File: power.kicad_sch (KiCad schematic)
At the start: 30 parts, among them U201 XC6206PxxxMR, U202 XR76208

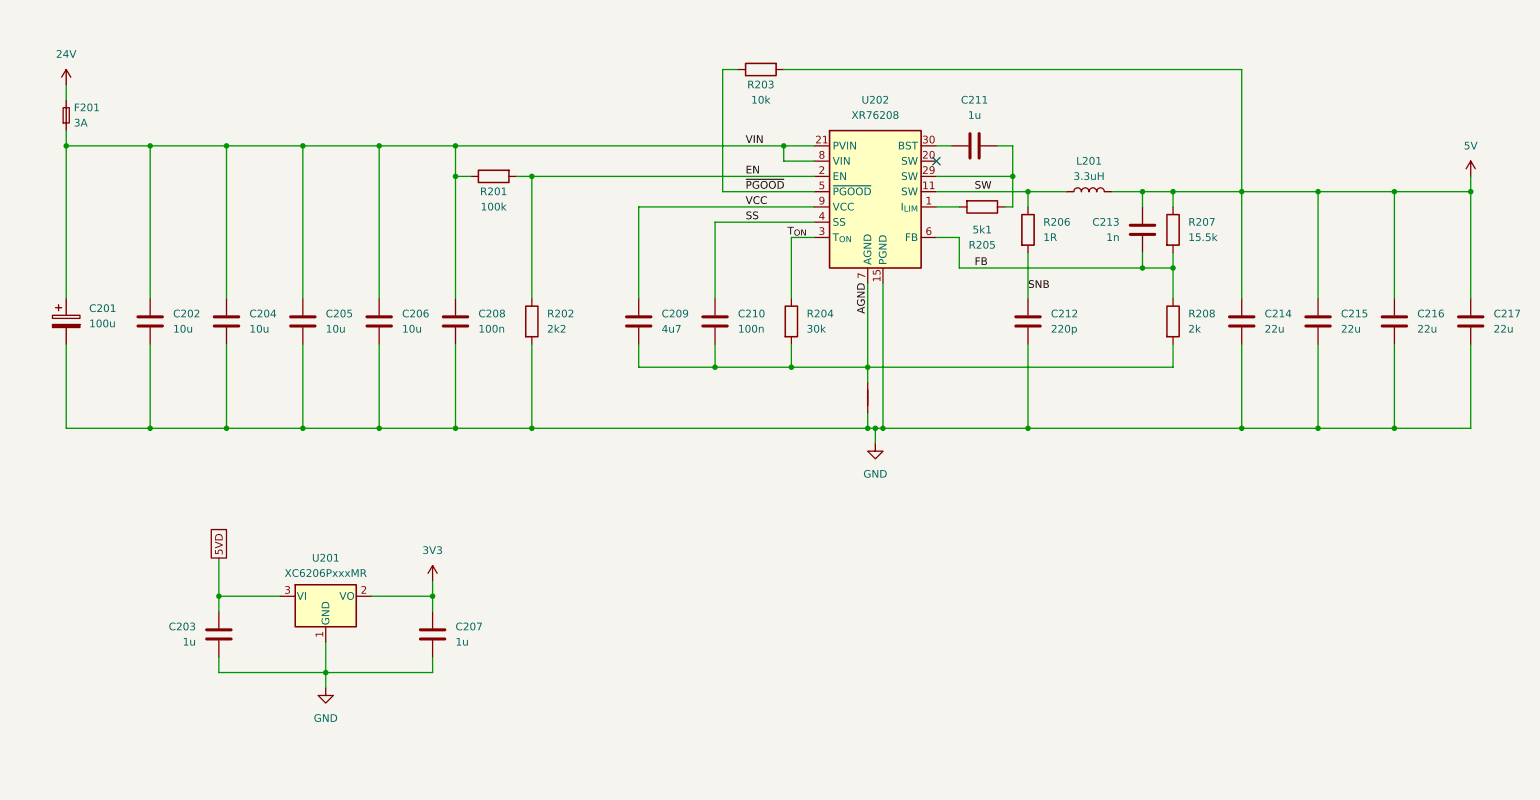
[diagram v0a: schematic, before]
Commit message: Schema improvements and CAN transceiver modification
- Improved schema layout for better readability and organization
- Connected CAN transceiver S-pin to GND for proper operation
- Updated PCB layout to reflect schema changes
- Enhanced component placement and routing clarity
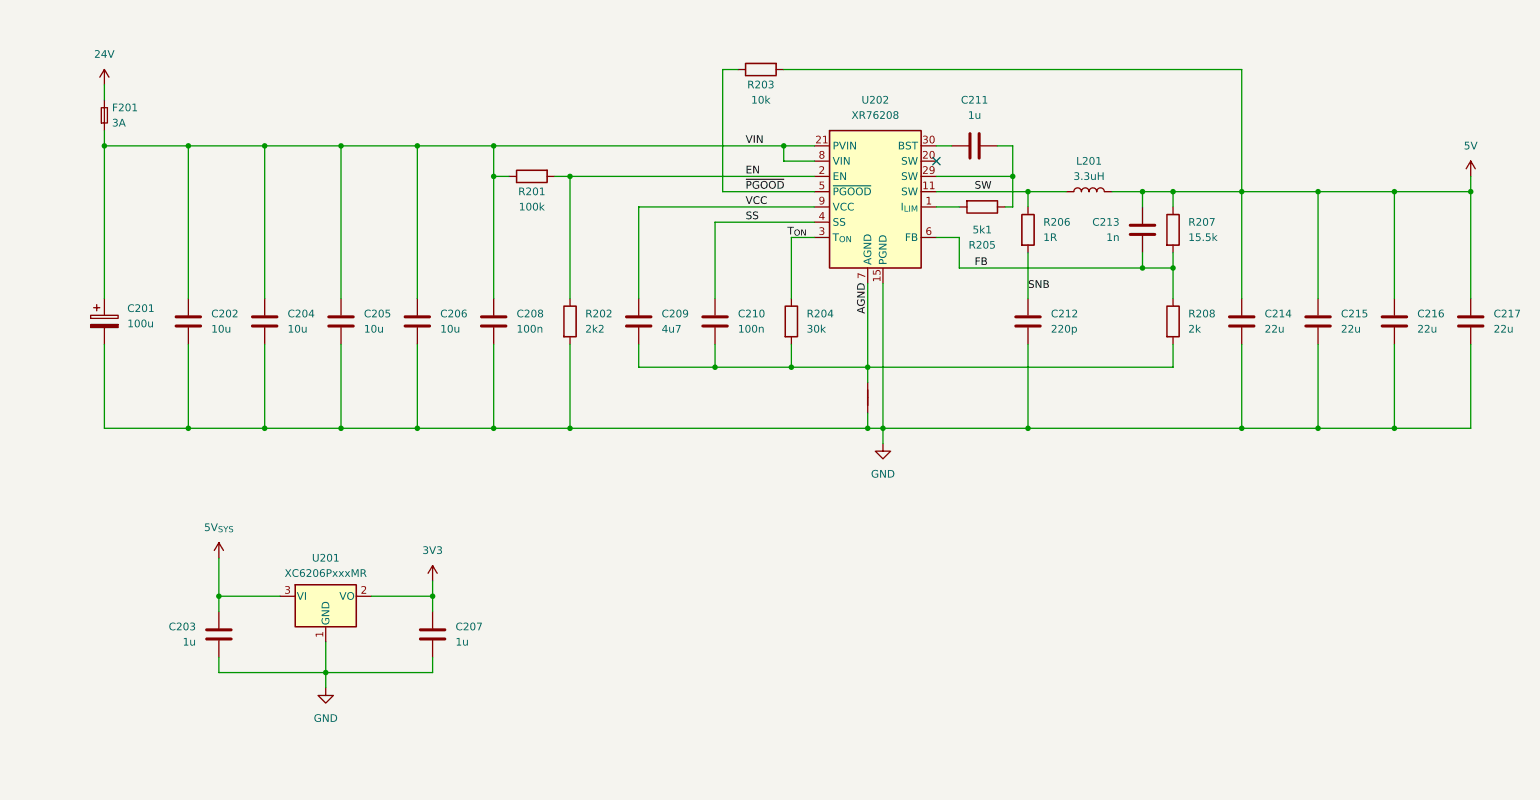
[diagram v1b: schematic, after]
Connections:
- net 5VD renamed 5V_{SYS}
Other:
- moved on the sheet: C201, C202, C204, C205, C206, C208, F201, R201, R202

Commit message: Rev 0.2: Major hardware improvements and production readiness
Hardware Improvements (Thanks to shx for schematic cleanup):
- Clean up schematic organization and structure
- Set CAN transceiver Silent pin to GND for stability
- Add status LEDs (yellow: 24V/5V/3.3V, green: MCU PB4)
- Replace jumpers with solder jumpers on bottom side
- Add jumpers to output PFETs for permanent-on without firmware
- Add robust test points for 5V/GND load testing
- Add optional heatsink for DC/DC converter on bottom
- Add 10µF capacitor for MCU on 3.3V rail

Component Optimizations:
- Replace 30kΩ with 33kΩ basic part for simplified BOM
- Change DC/DC feedback: 15.5kΩ15kΩ (new output: 5.1V)
- Upgrade CAN ESD protection: NUP2105LPESD1CAN
- Increase CAN termination resistor footprint: 04020603
- Switch USB hub supply from 5V to 3.3V per datasheet

Production Ready:
- Add all LCSC part numbers and rotations
- Generate complete production data package
- Improve PCB layout and button placement
- Create comprehensive changelog documentation
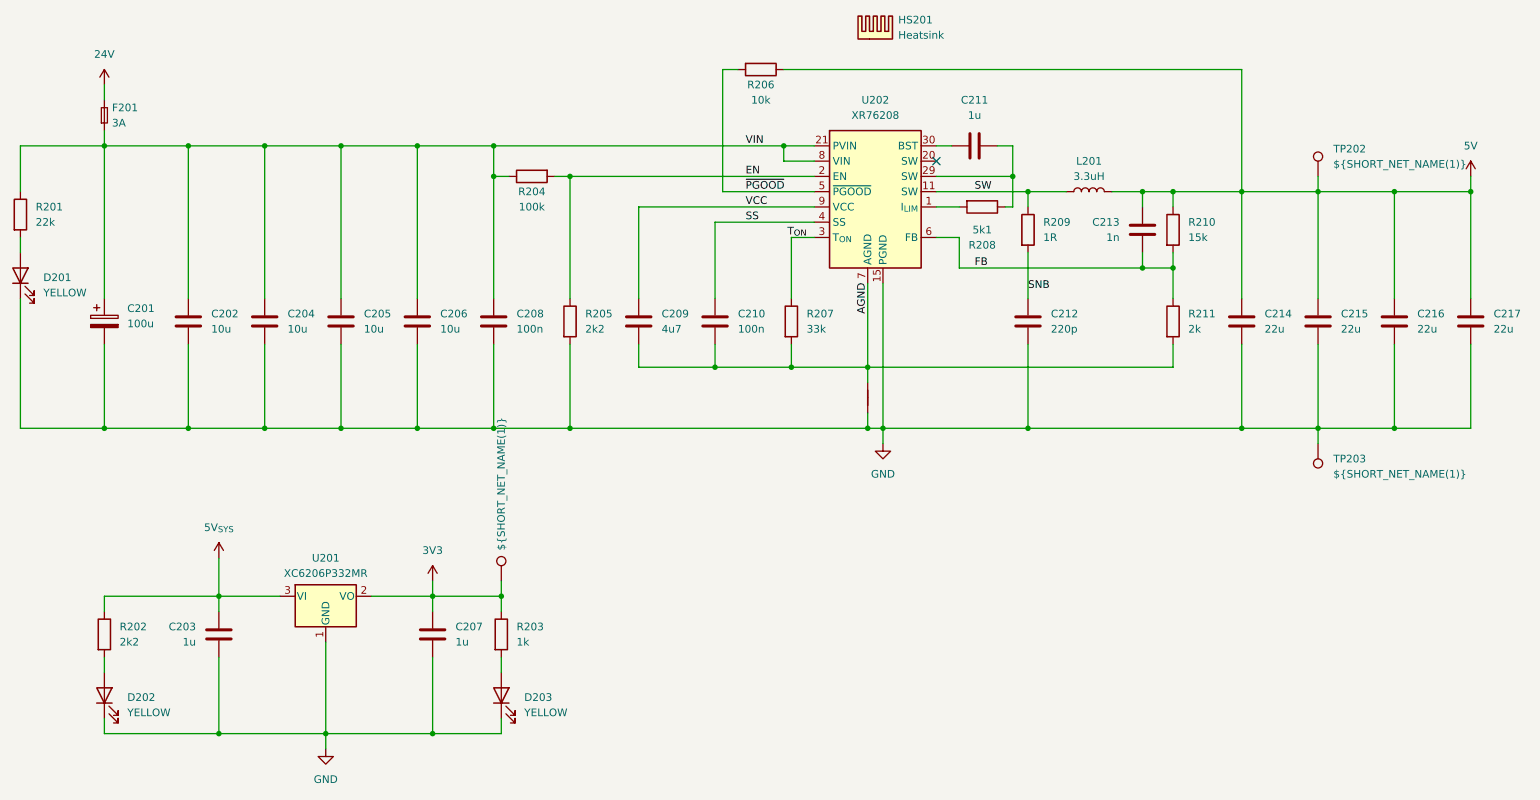
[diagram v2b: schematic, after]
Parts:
- added D201, D202, D203: YELLOW, LED_SMD:LED_0805_2012Metric, symbol Device:LED
- added HS201: Heatsink, project:HeatSink_9x9x5, symbol Mechanical:Heatsink
- added R201: 22k, Resistor_SMD:R_0402_1005Metric, symbol Device:R
- added R202: 2k2, Resistor_SMD:R_0402_1005Metric, symbol Device:R
- added R203: 1k, Resistor_SMD:R_0402_1005Metric, symbol Device:R
- added TP201: ${SHORT_NET_NAME(1)}, project:NAMED_TEST_POINT, symbol project:NamedTestPoint
- added TP202, TP203: ${SHORT_NET_NAME(1)}, TestPoint:TestPoint_Pad_D3.0mm, symbol Connector:TestPoint
- C203, C207, C211: LCSC Part # (none) -> C52923; Manufacturer Part # (none) -> CL05A105KA5NQNC
- C208, C210: LCSC Part # (none) -> C307331; Manufacturer Part # (none) -> CL05B104KB54PNC
- C212: LCSC Part # (none) -> C1603; Manufacturer Part # (none) -> CL10B221KB8NNNC
- C213: LCSC Part # (none) -> C1523; Manufacturer Part # (none) -> 0402B102K500NT
- C214, C215, C216, C217: LCSC Part # (none) -> C12891; Manufacturer Part # (none) -> CL31A226KAHNNNE
- F201: LCSC Part # (none) -> C163126; Manufacturer Part # (none) -> CFS12V3T3R00
- R204: renamed from R201; LCSC Part # (none) -> C25741; Manufacturer Part # (none) -> 0402WGF1003TCE
- R205: renamed from R202; LCSC Part # (none) -> C25879; Manufacturer Part # (none) -> 0402WGF2201TCE
- R206: renamed from R203; LCSC Part # (none) -> C25744; Manufacturer Part # (none) -> 0402WGF1002TCE
- R207: renamed from R204; value 30k -> 33k; LCSC Part # (none) -> C25779; Manufacturer Part # (none) -> 0402WGF3302TCE
- R208: renamed from R205; LCSC Part # (none) -> C25905; Manufacturer Part # (none) -> 0402WGF5101TCE
- R209: renamed from R206; LCSC Part # (none) -> C22936; Manufacturer Part # (none) -> 0603WAF100KT5E
- R210: renamed from R207; value 15.5k -> 15k; LCSC Part # (none) -> C25756; Manufacturer Part # (none) -> 0402WGF1502TCE
- R211: renamed from R208; LCSC Part # (none) -> C4109; Manufacturer Part # (none) -> 0402WGF2001TCE
- U201: value XC6206PxxxMR -> XC6206P332MR; LCSC Part # (none) -> C5446; Manufacturer Part # (none) -> XC6206P332MR-G
- U202: LCSC Part # (none) -> C555356; Manufacturer Part # (none) -> XR76208ELTR-F
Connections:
- net 3V3: now also R203.1, TP201.1
- net 5V: now also R206.1, TP202.1; no longer R206.2
- net 5V_{SYS}: now also R202.1
- net AGND: no longer U202.31 (AGND)
- net GND: now also D201.1 (K), D202.1 (K), D203.1 (K), TP203.1
- net VIN: now also R201.1
- net ~{PGOOD}: now also R206.2; no longer R206.1
- new net: D202.2 (A), R202.2
- new net: D203.2 (A), R203.2
- new net: D201.2 (A), R201.2
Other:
- moved on the sheet: R206
